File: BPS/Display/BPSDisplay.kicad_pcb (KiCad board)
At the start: 2 copper layers, 85 x 56 mm, 63 parts, among them J1 SWD, J2 Conn_02x06_Counter_Clockwise, J3 CAN_Out, J4 isoSPI_Display, J5 CarPowerConnector, P1 Conn_02x20_Odd_Even, SW1 Reset, U1 STM32F413RHTx, U2 CDSOT23-T24CAN, U3 ADM3055E, U4 LTC6820, U5 HX1188FNL, U6 PDS1-S12-S5, U7 NCP1117-3.3_SOT223, Y1 8M

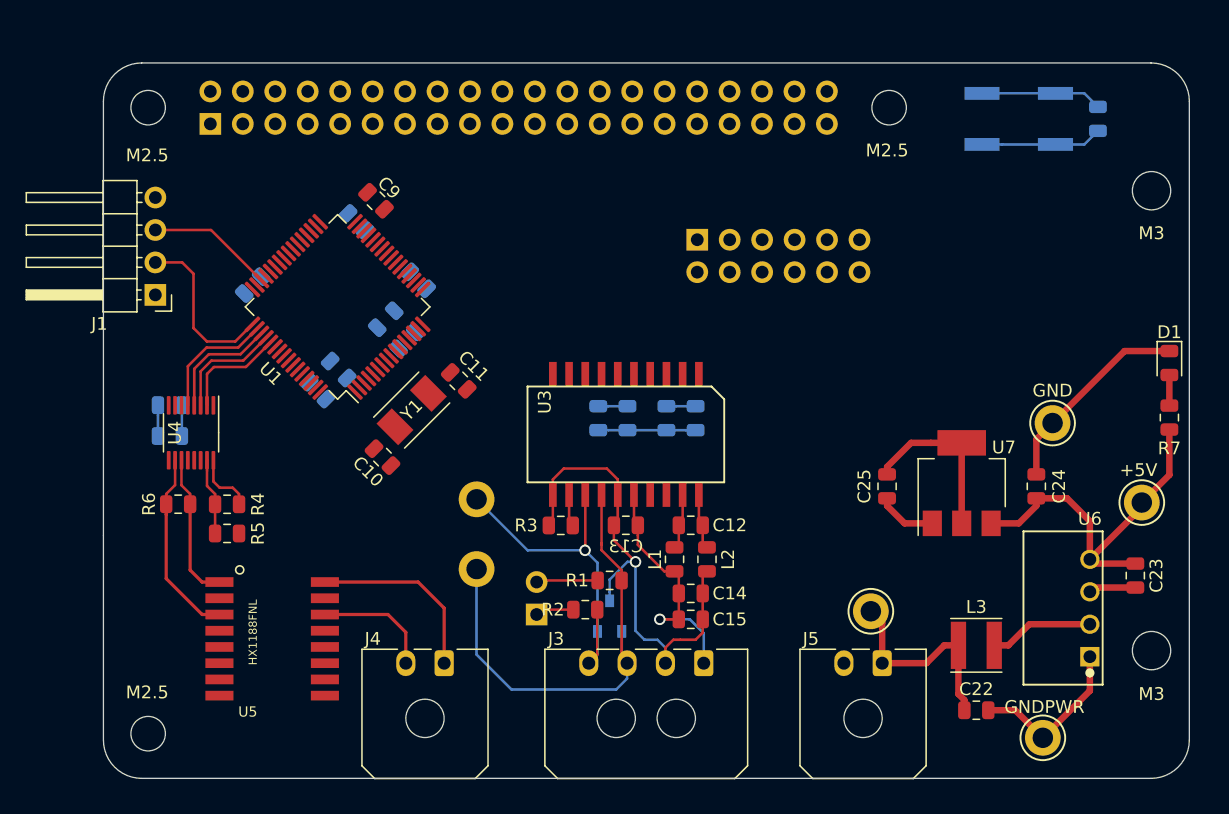
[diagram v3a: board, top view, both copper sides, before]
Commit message: Finish Display board, generate Gerbers.
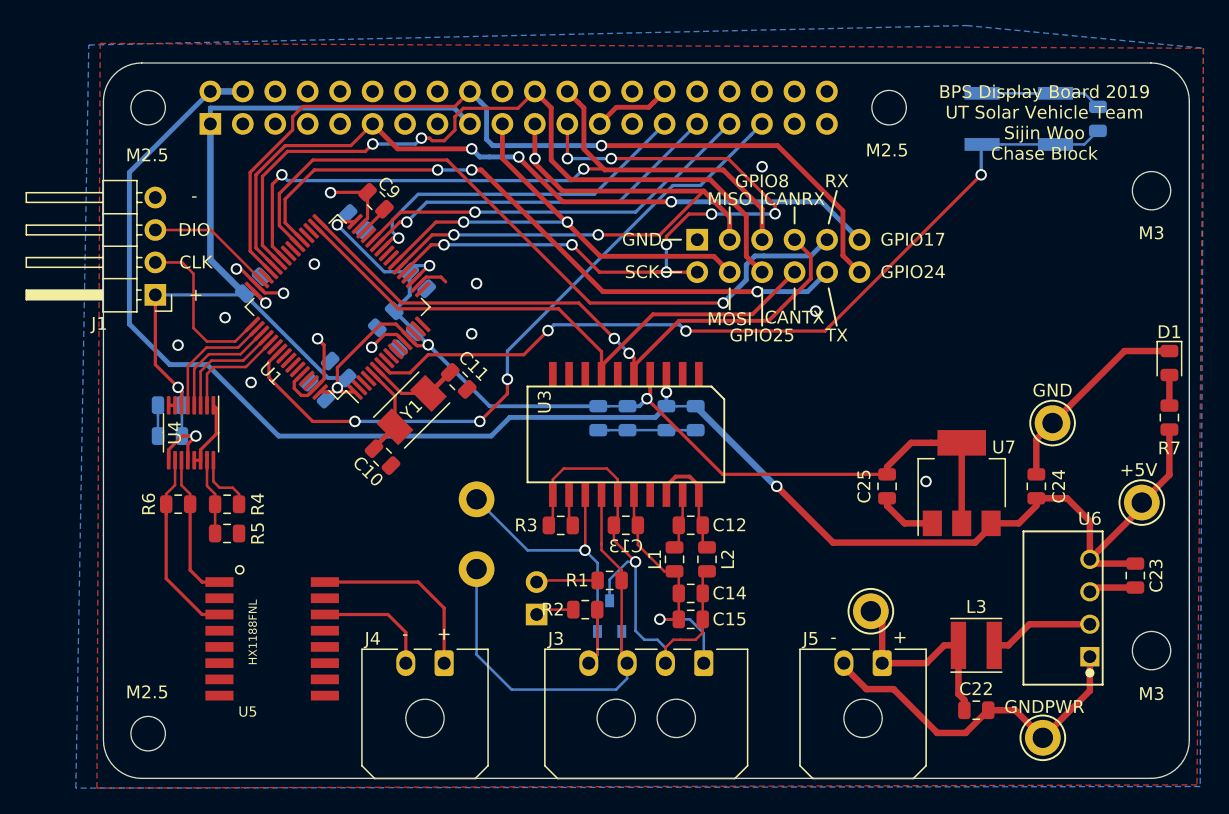
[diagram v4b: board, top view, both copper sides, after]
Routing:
- net +3V3: track 18.2 -> 170.8 mm, vias 0 -> 8
- net +5V: track 31.3 -> 132.2 mm, vias 0 -> 2
- net /GPIO24(GEN5): track 0.00 -> 68.7 mm, vias 0 -> 1
- net /GPIO17(GEN0): track 0.00 -> 60.5 mm, vias 0 -> 3
- net /GPIO25(GEN6): track 0.00 -> 60.1 mm, vias 0 -> 2
- net /GPIO11(SPI0_SCK): track 0.00 -> 58.6 mm, vias 0 -> 8
- net /GPIO8(SPI0_CE_N): track 0.00 -> 56.4 mm, vias 0 -> 2
- net /NRST: track 9.52 -> 65.9 mm, vias 0 -> 3
- net /USART6_RX: track 0.00 -> 55.9 mm, vias 0 -> 1
- net /GPIO19: track 0.00 -> 54.0 mm, vias 0 -> 3
- net /USART6_TX: track 0.00 -> 51.7 mm, vias 0 -> 3
- net /CAN2_RX: track 0.00 -> 51.2 mm, vias 0 -> 2
- net /GPIO9(SPI0_MISO): track 0.00 -> 48.1 mm, vias 0 -> 3
- net /CAN2_TX: track 0.00 -> 47.0 mm
- net /GPIO10(SPI0_MOSI): track 0.00 -> 39.0 mm, vias 0 -> 2
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- added copper zone on B.Cu, net GND
- added copper zone on F.Cu, net GND
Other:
- board text added: "+"
- board text added: "-"
- board text added: "BPS Display Board 2019 UT Solar Vehicle Team Sijin Woo Chase Block"
- board text added: "CANRX"
- board text added: "CANTX"
- board text added: "CLK"
- board text added: "DIO"
- board text added: "GPIO17"
- board text added: "GPIO24"
- board text added: "GPIO25"
- board text added: "GPIO8"
- board text added: "MISO"
- board text added: "MOSI"
- board text added: "RESET"
- board text added: "RX"
- board text added: "SCK"
- board text added: "TX"
